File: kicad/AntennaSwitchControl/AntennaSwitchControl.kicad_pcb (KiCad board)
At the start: 2 copper layers, 184.7 x 104.7 mm, 123 parts, among them J1 Conn_01x12_Socket, J2 Conn_01x12_Socket, J3 POWER, K1 AHQSH112LM100G, K10 AHQSH112LM100G, K11 AHQSH112LM100G, K12 AHQSH112LM100G, K13 AHQSH112LM100G, K14 AHQSH112LM100G, K15 AHQSH112LM100G, K16 AHQSH112LM100G, K2 AHQSH112LM100G, K3 AHQSH112LM100G, K4 AHQSH112LM100G, K5 AHQSH112LM100G, K6 AHQSH112LM100G, K7 AHQSH112LM100G, K8 AHQSH112LM100G, K9 AHQSH112LM100G, Q1 2N7000, Q10 2N7000, Q11 2N7000, Q12 2N7000, Q13 2N7000, Q14 2N7000, Q15 2N7000, Q16 2N7000, Q2 2N7000, Q3 2N7000, Q4 2N7000, Q5 2N7000, Q6 2N7000, Q7 2N7000, Q8 2N7000, Q9 2N7000, SW1 Mode Button, U1 PicoW, U3 L7805

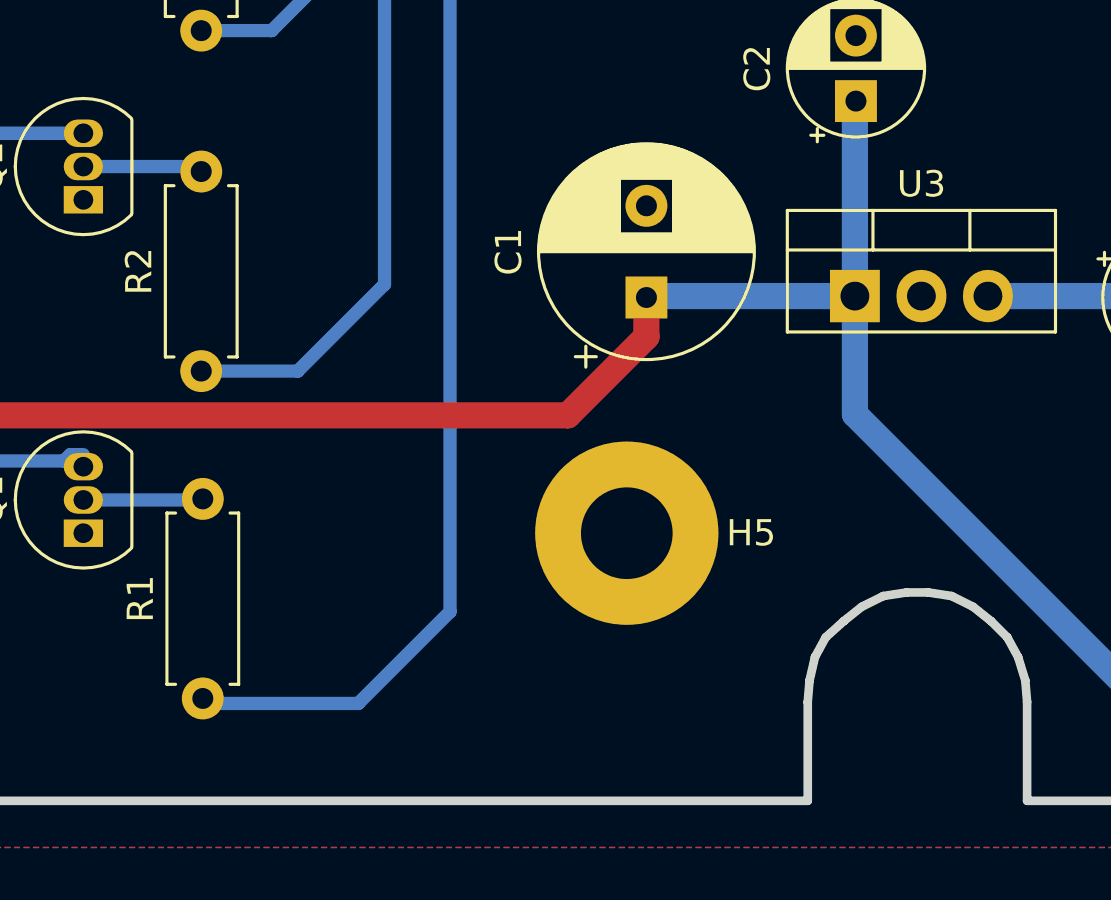
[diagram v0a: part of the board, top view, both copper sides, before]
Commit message: add BOM, clean up schematic
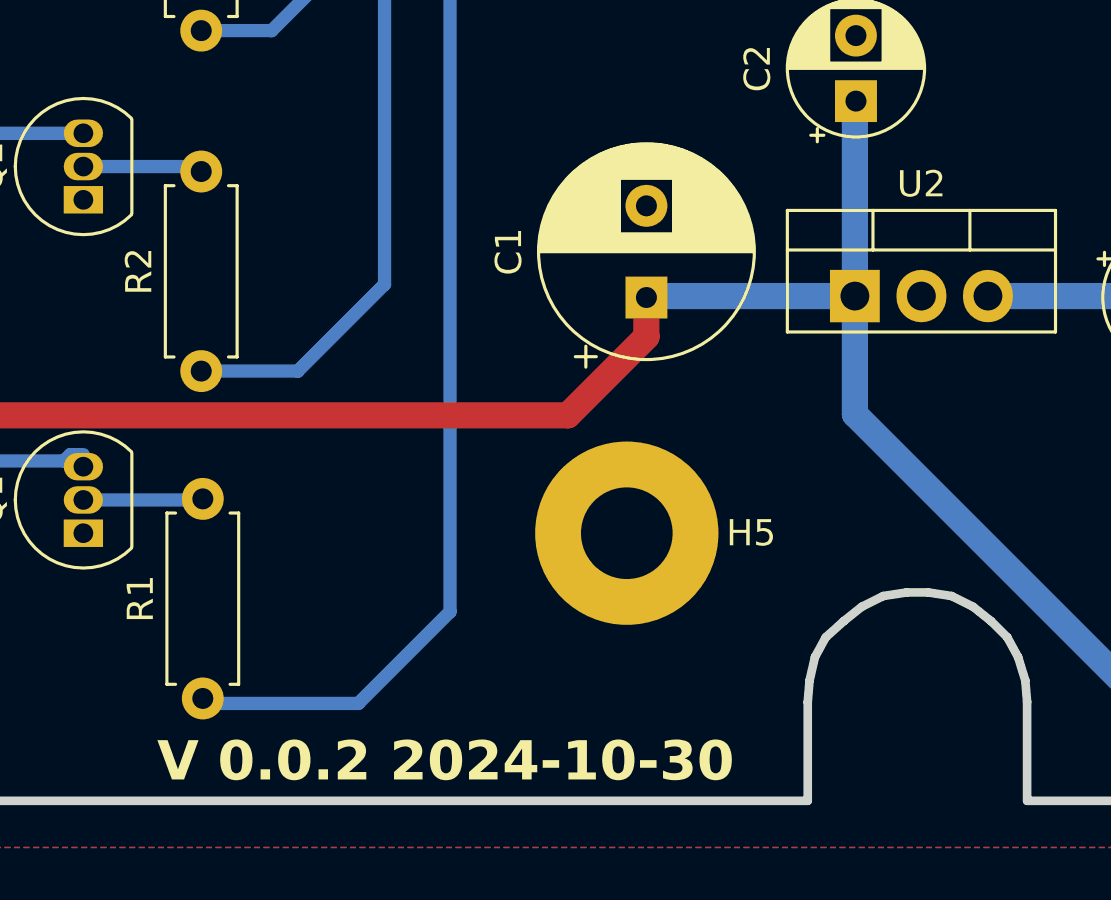
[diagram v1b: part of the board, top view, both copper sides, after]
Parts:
- R10: value 10 -> 100
- R22, R23, R24, R25, R26, R27, R28, R29, R30, R31, R32, R33, R34, R35, R36, R37: value 330 -> 1K
- renumbered U3 to U2
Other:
- board text added: "V 0.0.2 2024-10-30"

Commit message: # Conflicts: #	src/switch_control/http_server.py
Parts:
- removed G***: LOGO, parts:non-ionizing
- removed G***: LOGO, parts:non-ionizing-bigger
- added G1: LOGO, parts:non-ionizing-bigger, F.Cu at (62.2, 91.9)
- J1, J2: value Conn_01x12_Socket -> Terminal Block 12 terminal; footprint Library:705530116 -> Library:CUI_TBP04R1-500-12BE
- J3: footprint Library:705530001 -> Library:CUI_TBP04R1-500-02BE
- U1: footprint parts:RPi_PicoW_SMD_TH -> Library:RPi_PicoW_SMD_TH
- moved Ref** 169.0 mm to (62.5, 105.3), turned to 0 degrees
- moved SW1 107.0 mm to (183.3, 117.0), turned to 0 degrees
- moved D20 103.6 mm to (191.4, 122.7)
- moved R21 100.1 mm to (194.4, 122.7), turned to 0 degrees
- moved U1 75.1 mm to (210.4, 97.5), turned to -90 degrees
- moved R37 74.5 mm to (54.1, 67.0), turned to 0 degrees
- moved K1 73.5 mm to (54.1, 55.2), turned to 90 degrees
- moved R16 72.9 mm to (234.8, 75.0), turned to 180 degrees
- moved D1 72.7 mm to (54.1, 59.2), turned to 0 degrees
- moved R1 72.3 mm to (61.5, 75.0), turned to 180 degrees
- moved Q1 71.0 mm to (56.6, 71.3), turned to 0 degrees
- moved Q16 70.4 mm to (229.6, 71.3), turned to 0 degrees
- moved D21 70.2 mm to (232.2, 63.2), turned to 180 degrees
- moved D18 68.6 mm to (138.0, 105.0), turned to 180 degrees
- moved D36 67.9 mm to (59.1, 63.2)
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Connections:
- SW1 pad 2: Net-(U1-GPIO1) -> /MODE
- U1 pad 1: /BLINKY -> /B8
- U1 pad 10: /A7 -> /B1
- U1 pad 11: /A6 -> /A8
- U1 pad 12: /A5 -> /A7
- U1 pad 14: /A4 -> /A6
- U1 pad 15: /A3 -> /A5
- U1 pad 16: /A2 -> /A4
- U1 pad 17: /A1 -> /A3
- U1 pad 19: unconnected-(U1-GPIO14-Pad19)_1 -> /A2
- U1 pad 2: Net-(U1-GPIO1) -> /B7
- U1 pad 20: unconnected-(U1-GPIO15-Pad20)_1 -> /A1
- U1 pad 21: /B8 -> /MODE
- U1 pad 22: /B7 -> /BLINKY
- U1 pad 24: /B6 -> unconnected-(U1-GPIO18-Pad24)
- U1 pad 25: /B5 -> unconnected-(U1-GPIO19-Pad25)
- U1 pad 26: /B4 -> unconnected-(U1-GPIO20-Pad26)_1
- U1 pad 27: /B3 -> unconnected-(U1-GPIO21-Pad27)
- U1 pad 31: /B2 -> unconnected-(U1-GPIO26_ADC0-Pad31)_1
- U1 pad 32: /B1 -> unconnected-(U1-GPIO27_ADC1-Pad32)_1
- U1 pad 36: +3.3V -> unconnected-(U1-3V3-Pad36)
- U1 pad 4: unconnected-(U1-GPIO2-Pad4) -> /B6
- U1 pad 5: unconnected-(U1-GPIO3-Pad5) -> /B5
- U1 pad 6: unconnected-(U1-GPIO4-Pad6) -> /B4
- U1 pad 7: unconnected-(U1-GPIO5-Pad7) -> /B3
- U1 pad 9: /A8 -> /B2
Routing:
- net +12V: track 664.3 -> 523.7 mm
- net Net-(D18-K): track 6.65 -> 99.6 mm
- net /A5: track 21.3 -> 98.8 mm
- net /A3: track 39.2 -> 116.7 mm
- net /A4: track 30.3 -> 107.7 mm
- net /A2: track 48.8 -> 122.8 mm
- net /A1: track 58.9 -> 131.4 mm
- net /A6: track 20.3 -> 89.8 mm
- net /A7: track 29.6 -> 83.3 mm
- net +5V: track 67.8 -> 25.3 mm
- net /OA1: track 70.0 -> 27.5 mm
- net /A8: track 41.2 -> 74.4 mm
- net /B8: track 40.7 -> 13.7 mm
- net /OA2: track 44.7 -> 20.0 mm
- net /OB8: track 59.8 -> 37.3 mm
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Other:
- board text added: "Antenna Switch Control"
- board text added: "N1KDO 2025"
- board text added: "V 0.0.3 2025-02-01"
- board text removed: "2x8 Control"
- board text removed: "N1KDO 2024"
- board text removed: "V 0.0.2 2024-10-30"
